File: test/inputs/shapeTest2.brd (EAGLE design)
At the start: 2 parts

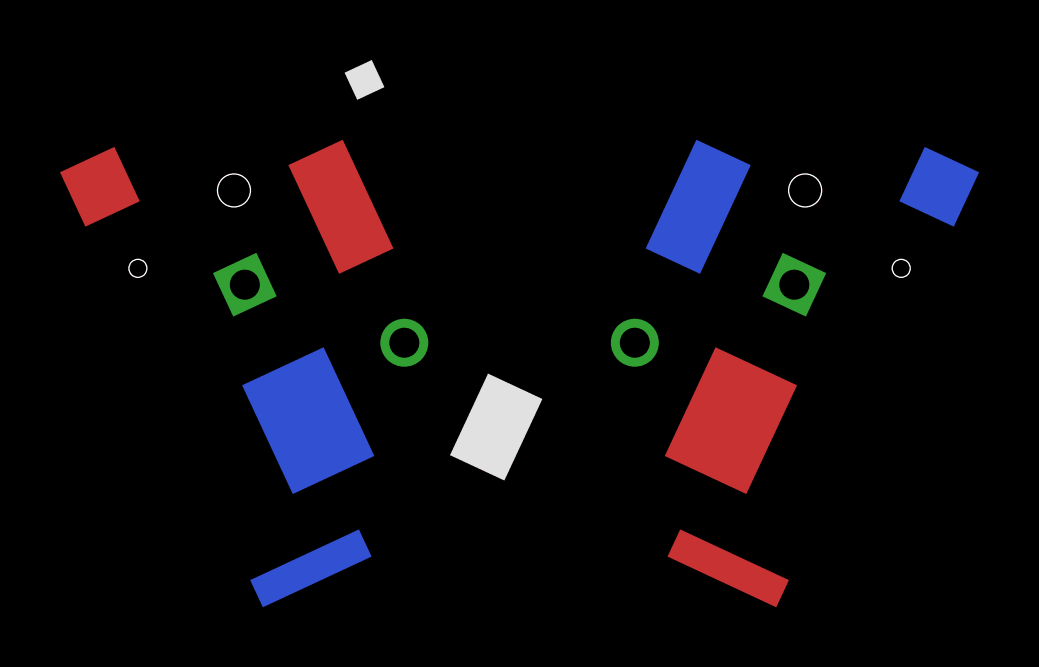
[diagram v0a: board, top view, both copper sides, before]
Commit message: Improvements for ShapelySwoop to use DRU
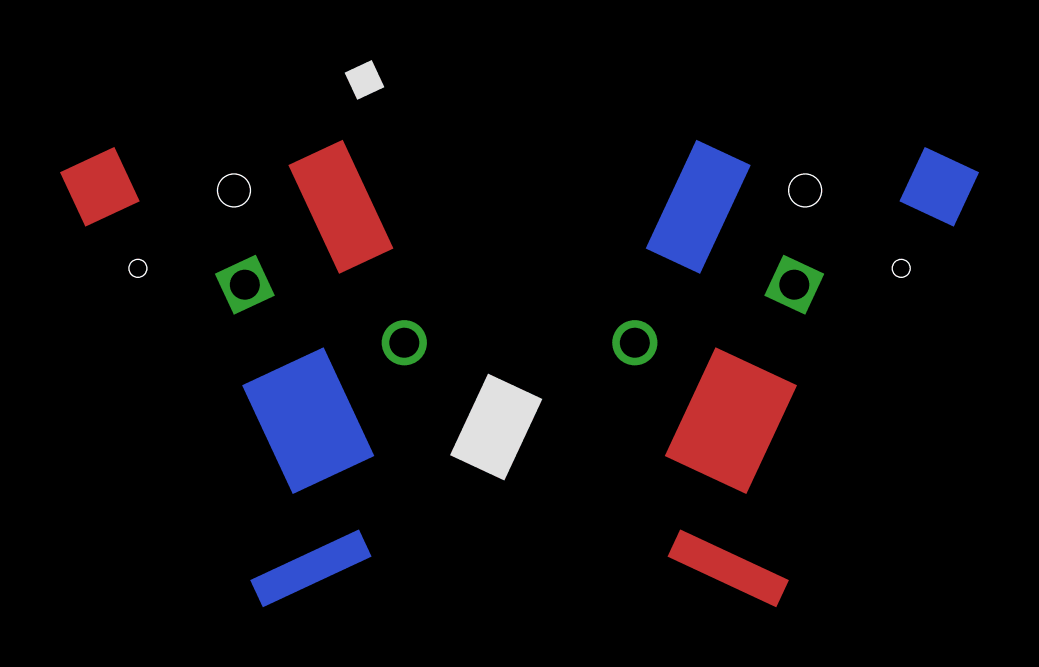
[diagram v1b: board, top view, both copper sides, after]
